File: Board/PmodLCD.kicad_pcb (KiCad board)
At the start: 2 copper layers, 88.9 x 29.2 mm, 31 parts, among them IC1 FAN533B, P1 PMOD, P2 PMOD, P3 PMOD, P4 PMOD, P5 LCD_BOTTOM, P6 LCD_TOP, P7 TOUCH, SW1 SPST-4

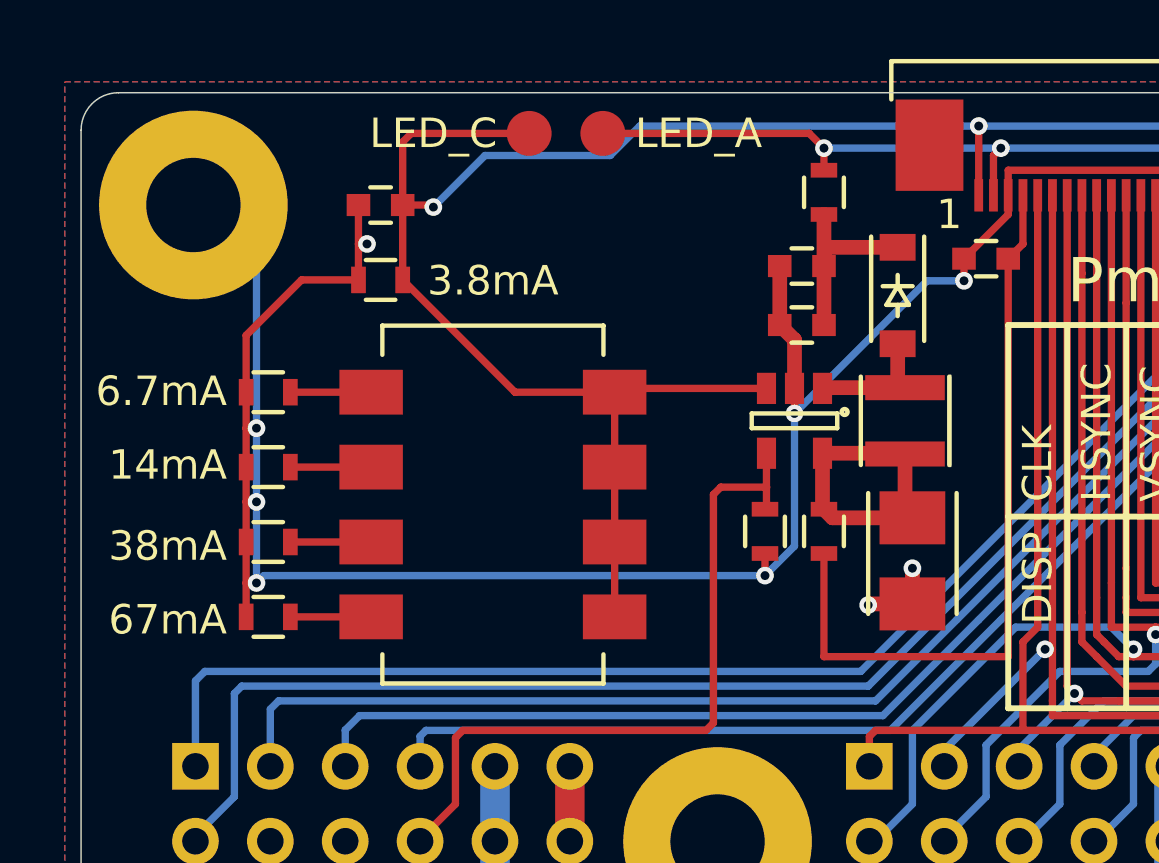
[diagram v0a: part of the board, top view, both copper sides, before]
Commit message: Changed Switch Footprint
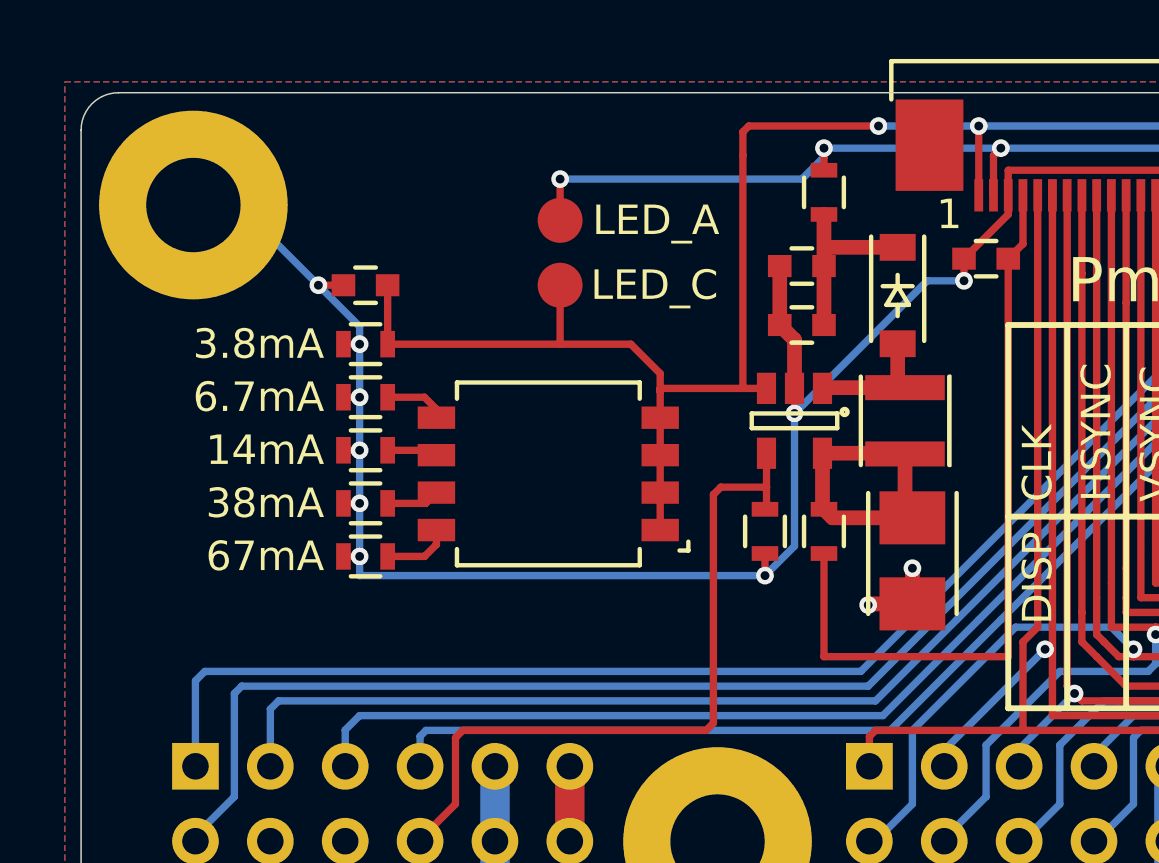
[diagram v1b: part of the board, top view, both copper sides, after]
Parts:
- SW1: footprint Misc:ADF04S04 -> Misc:GDH04S04
- moved W6 5.26 mm to (121.8, 82.4)
- moved R2 3.88 mm to (115.2, 91.6)
- moved R3 3.55 mm to (115.2, 89.8)
- moved R4 3.35 mm to (115.2, 88.0)
- moved R5 3.30 mm to (115.2, 86.2)
- moved W5 3.29 mm to (121.8, 80.2)
- moved C4 2.77 mm to (115.2, 82.4)
- moved R1 2.24 mm to (115.2, 84.4)
- moved SW1 2.15 mm to (121.4, 88.8)
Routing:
- net GND: track 218.9 -> 203.0 mm, vias 10 -> 12
- net /LED_C: track 102.1 -> 90.2 mm
- net /LED_A: track 62.4 -> 65.6 mm, vias 3 -> 4
- net Net-(R4-Pad1): track 2.74 -> 1.72 mm
- net Net-(R3-Pad1): track 2.74 -> 1.81 mm
- net Net-(R5-Pad1): track 2.74 -> 2.11 mm
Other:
- board text added: "PmodLCD Rev. 1, 2016 twam.info CC-BY-SA 4.0"
